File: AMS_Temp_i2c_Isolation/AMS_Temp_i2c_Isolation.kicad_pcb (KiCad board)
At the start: 2 copper layers, 80 x 50 mm, 49 parts, among them J1 Conn_01x02_Pin, J10 Conn_01x02_Pin, J2 Conn_01x02_Pin, J3 Conn_01x02_Pin, J4 Conn_01x04_Pin, J5 Conn_01x10_Socket, J6 Conn_01x04_Pin, J8 Conn_01x02_Pin, J9 Conn_01x02_Pin, U1 ADuM1250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

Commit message: 部品配置
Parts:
- added J4: JST_XH_S4B-XH-A_1x04_P2.50mm_Horizontal_Silk, MyFootprints:JST_XH_S4B-XH-A_1x04_P2.50mm_Horizontal_Silk, B.Cu at (159.0, 79.5)
- moved J1 31.3 mm to (131.8, 110.5), turned to 0 degrees
- moved J8 31.2 mm to (116.2, 79.5), turned to 180 degrees
- moved R8 23.7 mm to (132.5, 106.8), turned to 180 degrees
- moved R11 23.0 mm to (115.4, 83.2), turned to 0 degrees
- moved R3 20.1 mm to (155.0, 75.2), turned to -90 degrees
- moved R4 17.6 mm to (155.0, 78.4), turned to -90 degrees
- moved R9 11.4 mm to (133.4, 83.2)
- moved J10 9.00 mm to (122.8, 110.5)
- moved J9 9.00 mm to (113.8, 110.5)
- moved C7 8.51 mm to (121.5, 95.2)
- moved J2 8.00 mm to (134.2, 79.5)
- moved J3 8.00 mm to (125.2, 79.5)
- moved R12 7.94 mm to (114.6, 106.8)
- moved R10 6.45 mm to (124.4, 83.2)
- moved L1 5.39 mm to (169.0, 100.0)
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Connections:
- net Net-(D4-K) renamed /_+Vin
- net Net-(PS1-+Vin) renamed /+Vin
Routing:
- net +12V: track 0.00 -> 41.1 mm
- net +5VD: track 0.00 -> 26.2 mm
- net /+Vin: track 0.00 -> 24.2 mm
- net /SCL2: track 0.00 -> 20.5 mm
- net +5VA: track 0.00 -> 20.1 mm, vias 0 -> 3
- net /SDA2: track 0.00 -> 19.9 mm
- net /_+Vin: track 0.00 -> 12.7 mm
- net GNDD: track 0.00 -> 9.57 mm
- net GNDA: track 0.00 -> 9.52 mm
- net /AREF: track 0.00 -> 1.96 mm, vias 0 -> 1
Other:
- board text added: "+12V"
- board text added: "A0"
- board text added: "A1"
- board text added: "A2"
- board text added: "A3"
- board text added: "A6"
- board text added: "A7"
- board text added: "CTS"
- board text added: "DTR"
- board text added: "GND"
- board text added: "INPUT"
- board text added: "INSIDE of SEGMENT"
- board text added: "MISO"
- board text added: "MOSI"
- board text added: "OUTPUT"
- board text added: "OUTSIDE of SEGMENT"
- board text added: "RST"
- board text added: "RXI"
- board text added: "SCK"
- board text added: "SCL"
- board text added: "SDA"
- board text added: "TXO"
- board text added: "VCC"

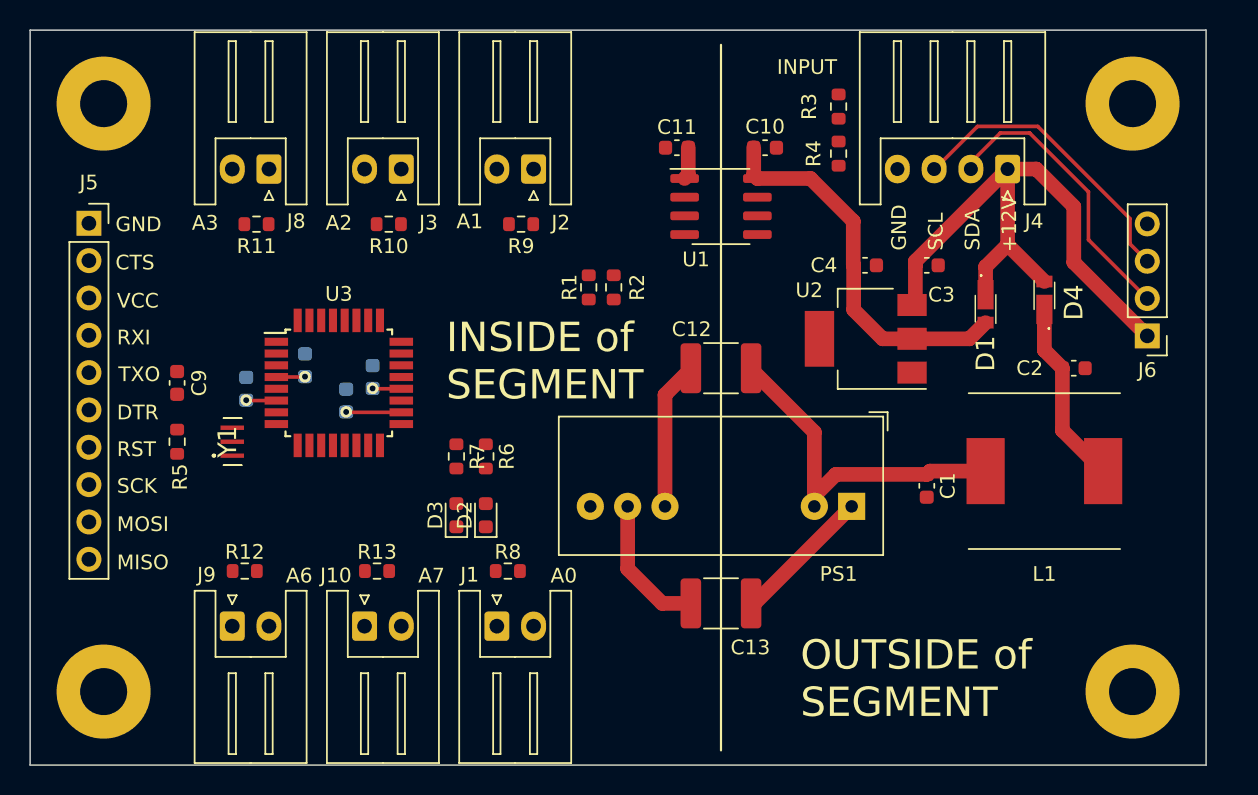
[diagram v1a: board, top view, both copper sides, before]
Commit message: 回路図修正, パターン作成
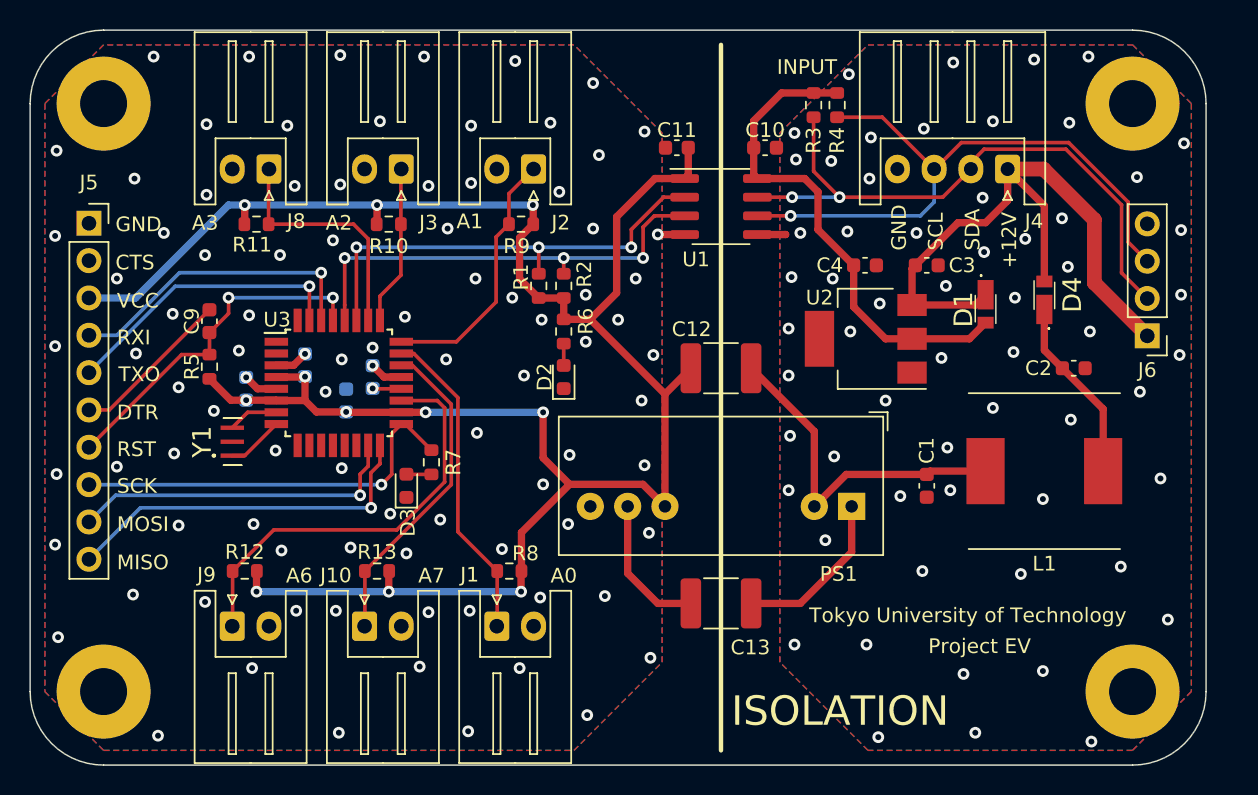
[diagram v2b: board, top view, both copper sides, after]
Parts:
- moved D2 10.8 mm to (136.3, 93.6)
- moved R6 10.0 mm to (136.3, 90.5)
- moved R5 5.55 mm to (112.2, 92.9)
- moved C9 4.74 mm to (112.2, 89.8)
- moved D3 3.94 mm to (125.6, 101.0)
- moved R1 3.40 mm to (134.6, 87.4)
- moved R2 3.40 mm to (136.3, 87.4)
- moved R4 3.30 mm to (154.9, 75.1)
- moved R7 1.75 mm to (127.3, 99.4)
- moved R3 1.70 mm to (153.3, 75.1)
- moved R8 0.10 mm to (132.6, 106.8)
- turned R9 to 180 degrees
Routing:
- net +5VA: track 20.1 -> 150.1 mm, vias 3 -> 11
- net /SDA1: track 0.00 -> 31.2 mm, vias 0 -> 3
- net /SCL1: track 0.00 -> 30.9 mm, vias 0 -> 3
- net /Sens5: track 0.00 -> 28.9 mm
- net /SCK: track 0.00 -> 27.4 mm, vias 0 -> 1
- net /MISO: track 0.00 -> 25.2 mm, vias 0 -> 1
- net /RESET: track 0.00 -> 23.9 mm, vias 0 -> 2
- net /MOSI: track 0.00 -> 22.8 mm, vias 0 -> 1
- net /SCL2: track 20.5 -> 42.9 mm, vias 0 -> 1
- net /Sens6: track 0.00 -> 22.0 mm
- net /Sens1: track 0.00 -> 21.8 mm
- net /SDA2: track 19.9 -> 41.2 mm, vias 0 -> 2
- net /RXI: track 0.00 -> 20.8 mm, vias 0 -> 1
- net /TXO: track 0.00 -> 19.8 mm, vias 0 -> 1
- net /Sens2: track 0.00 -> 17.7 mm
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- added copper zone on B.Cu, net GNDA
- added copper zone on F.Cu, net GNDA
- added copper zone on B.Cu, net GNDD
- added copper zone on F.Cu, net GNDD
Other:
- outline, holes or cut-outs redrawn
- board text added: "ISOLATION"
- board text added: "Project EV"
- board text added: "Tokyo University of Technology"
- board text removed: "INSIDE of SEGMENT"
- board text removed: "OUTSIDE of SEGMENT"

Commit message: パターン作成
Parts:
- moved C7 0.20 mm to (121.7, 95.2)
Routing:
- net GNDD: vias 60 -> 64
- net GNDA: vias 92 -> 100

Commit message: 修正とパターン完成
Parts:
- removed C12, C13: 220pF/3kV, Capacitor_SMD:C_1812_4532Metric
- R10, R11, R12, R13, R8, R9: footprint Resistor_SMD:R_0603_1608Metric -> Resistor_SMD:R_0805_2012Metric
- moved R9 1.08 mm to (132.4, 83.6)
- moved R11 0.41 mm to (115.3, 83.6)
- moved R12 0.41 mm to (114.7, 106.4)
- moved R13 0.41 mm to (123.7, 106.4)
- moved R8 0.41 mm to (132.7, 106.4)
- moved R10 0.40 mm to (124.4, 83.6)
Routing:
- net GNDD: track 13.3 -> 1.93 mm
- net /+Vin: track 23.8 -> 12.6 mm
- net GNDA: track 18.4 -> 8.74 mm, vias 100 -> 108
- net +5VA: track 150.1 -> 154.6 mm
- net /SCL1: track 30.9 -> 30.2 mm
- net /SDA1: track 31.2 -> 30.5 mm
- net /Sens4: track 16.5 -> 16.0 mm

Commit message: ベタ表面修正
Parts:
- moved C4 0.60 mm to (156.2, 86.0)
- moved C3 0.20 mm to (161.2, 86.0)
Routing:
- net +12V: track 43.7 -> 37.9 mm
- net +5VD: track 34.1 -> 38.7 mm
- net GNDA: track 8.74 -> 11.4 mm, vias 108 -> 105
- net GNDD: track 1.93 -> 3.25 mm
- net /Sens5: track 28.8 -> 29.6 mm
- net /Sens6: track 22.5 -> 23.3 mm

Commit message: 修正
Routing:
- net GNDA: vias 105 -> 103

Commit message: 修正
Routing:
- net +5VA: track 154.6 -> 153.5 mm

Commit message: 修正
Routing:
- net GNDD: vias 64 -> 65
